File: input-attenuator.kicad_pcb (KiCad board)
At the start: 2 copper layers, 90.2 x 55.8 mm, 100 parts, among them J1 DC_INTF, J2 DC_INTF, J3 RX, J4 ANT, J5 TX, K1 EE2-5TNU-L, K2 EE2-5TNU-L, K3 EE2-5TNU-L, K4 EE2-5TNU-L, Q1 BC858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

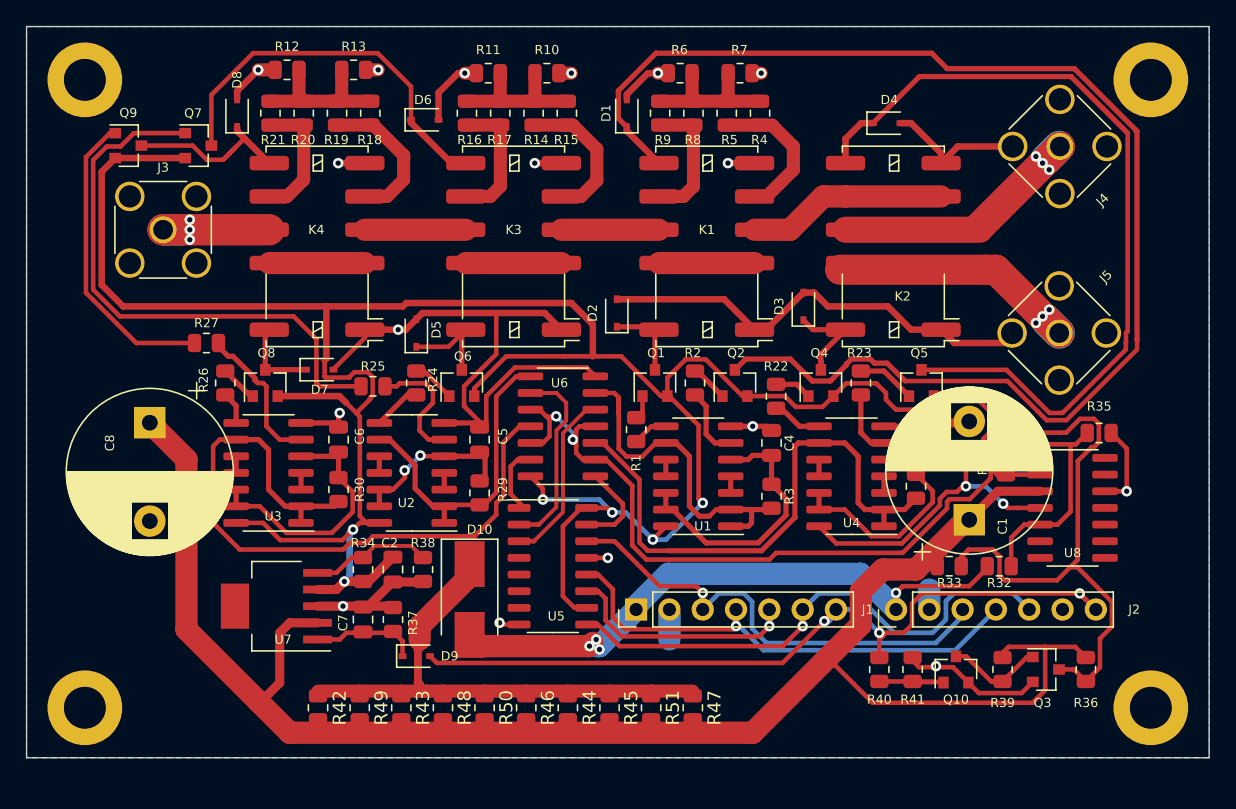
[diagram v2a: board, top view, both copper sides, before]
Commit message: Added regulator heat sink tab and module description on FCu
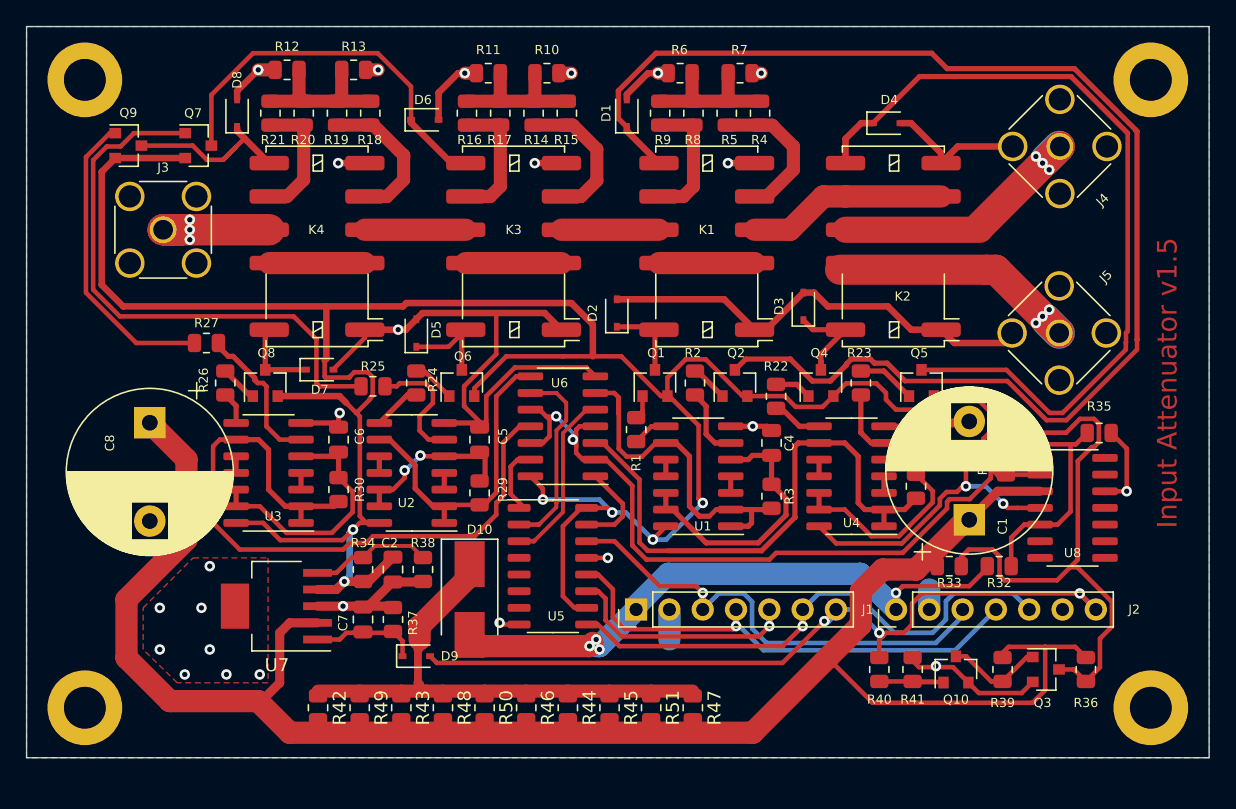
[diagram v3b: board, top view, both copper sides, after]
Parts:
- U7: footprint Package_TO_SOT_SMD:SOT-223-6 -> Package_TO_SOT_SMD:SOT-223-6_TabPin3
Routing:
- net /Vin2: track 135.0 -> 140.4 mm
- net GND: vias 17 -> 25
- added copper zone on F.Cu, net GND
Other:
- board text added: "Input Attenuator v1.5"
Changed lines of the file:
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@@
     )
   )
-  (footprint "Package_TO_SOT_SMD:SOT-223-6" (layer "F.Cu")
+  (footprint "Package_TO_SOT_SMD:SOT-223-6_TabPin3" (layer "F.Cu")
     (at 82.55 69.088 180)
     (descr "module CMS SOT223 6 pins, http://www.ti.com/lit/ds/symlink/tps737.pdf")
@@
     (property "Sheetname" "")
     (attr smd)
-    (fp_text reference "U7" (at -0.508 -2.54) (layer "F.SilkS")
-      (effects (font (size 0.7 0.7) (thickness 0.12)))
+    (fp_text reference "U7" (at -0.0375 -4.5 180) (layer "F.SilkS")
+      (effects (font (size 1 1) (thickness 0.15)))
     )
-    (fp_text value "TPS7A4501DCQT" (at -0.0375 4.5) (layer "F.Fab")
+    (fp_text value "TPS7A4501DCQT" (at -0.0375 4.5 180) (layer "F.Fab")
       (effects (font (size 1 1) (thickness 0.15)))
     )
-    (fp_text user "${REFERENCE}" (at 0 0 90) (layer "F.Fab")
-      (effects (font (size 0.7 0.7) (thickness 0.12)))
+    (fp_text user "${REFERENCE}" (at 0 0 270) (layer "F.Fab")
+      (effects (font (size 0.8 0.8) (thickness 0.12)))
     )
-    (fp_line (start -4.1375 -3.41) (end 1.8725 -3.41) (layer "F.SilkS") (width 0.12))
-    (fp_line (start 1.8725 3.41) (end 1.8725 2.15) (layer "F.SilkS") (width 0.12))
     (fp_line (start 1.8725 -3.41) (end 1.8725 -2.15) (layer "F.SilkS") (width 0.12))
+    (fp_line (start -4.1375 -3.41) (end 1.8725 -3.41) (layer "F.SilkS") (width 0.12))
     (fp_line (start -1.8875 3.41) (end 1.8725 3.41) (layer "F.SilkS") (width 0.12))
-    (fp_line (start 4.49 3.6) (end 4.49 -3.6) (layer "F.CrtYd") (width 0.05))
+    (fp_line (start 1.8725 3.41) (end 1.8725 2.15) (layer "F.SilkS") (width 0.12))
     (fp_line (start -4.49 -3.6) (end -4.49 3.6) (layer "F.CrtYd") (width 0.05))
-    (fp_line (start 4.49 3.6) (end -4.49 3.6) (layer "F.CrtYd") (width 0.05))
     (fp_line (start -4.49 -3.6) (end 4.49 -3.6) (layer "F.CrtYd") (width 0.05))
+    (fp_line (start 4.49 3.6) (end 4.49 -3.6) (layer "F.CrtYd") (width 0.05))
+    (fp_line (start 4.49 3.6) (end -4.49 3.6) (layer "F.CrtYd") (width 0.05))
+    (fp_line (start -0.8375 -3.35) (end 1.8125 -3.35) (layer "F.Fab") (width 0.1))
     (fp_line (start -1.8875 -2.3) (end -1.8875 3.35) (layer "F.Fab") (width 0.1))
     (fp_line (start 1.8125 -3.35) (end 1.8125 3.35) (layer "F.Fab") (width 0.1))
-    (fp_line (start -0.8375 -3.35) (end 1.8125 -3.35) (layer "F.Fab") (width 0.1))
     (fp_line (start -1.8875 3.35) (end 1.8125 3.35) (layer "F.Fab") (width 0.1))
     (fp_line (start -1.8875 -2.3) (end -0.8375 -3.35) (layer "F.Fab") (width 0.1))
@@
     (pad "3" smd rect (at -3.1375 0 180) (locked) (size 2.2 0.6) (layers "F.Cu" "F.Paste" "F.Mask")
       (net 11 "GND") (pinfunction "GND") (pintype "power_in"))
+    (pad "3" smd rect (at 3.1625 0 180) (locked) (size 2.15 3.45) (layers "F.Cu" "F.Paste" "F.Mask")
+      (net 11 "GND") (pinfunction "GND") (pintype "power_in"))
     (pad "4" smd rect (at -3.1375 1.27 180) (locked) (size 2.2 0.6) (layers "F.Cu" "F.Paste" "F.Mask")
       (net 1 "+5V") (pinfunction "OUT") (pintype "power_out"))
     (pad "5" smd rect (at -3.1375 2.54 180) (locked) (size 2.2 0.6) (layers "F.Cu" "F.Paste" "F.Mask")
       (net 81 "Net-(R34-Pad1)") (pinfunction "ADJ") (pintype "bidirectional"))
-    (pad "6" smd rect (at 3.1625 0 180) (locked) (size 2.15 3.45) (layers "F.Cu" "F.Paste" "F.Mask"))
-    (model "${KISYS3DMOD}/Package_TO_SOT_SMD.3dshapes/SOT-223-6.wrl"
+    (model "${KICAD6_3DMODEL_DIR}/Package_TO_SOT_SMD.3dshapes/SOT-223-6.wrl"
       (offset (xyz 0 0 0))
       (scale (xyz 1 1 1))
@@
     (fp_circle (center 0 0) (end 3.1 0) (layer "F.CrtYd") (width 0.05) (fill none))
     (pad "1" thru_hole circle (at 0 0) (locked) (size 5.7 5.7) (drill 3.2) (layers *.Cu *.Mask)
-      (net 11 "GND") (pinfunction "1"))
+      (net 11 "GND") (pinfunction "1") (pintype "input"))
   )
   (footprint "Diode_SMD:D_SOD-323" (layer "F.Cu")
@@
   )
   (gr_rect (start 63.5 24.892) (end 153.67 80.645) (layer "Edge.Cuts") (width 0.05) (fill none))
+  (gr_text "Input Attenuator v1.5" (at 150.495 52.07 90) (layer "F.Cu")
+    (effects (font (size 1.5 1.5) (thickness 0.3)))
+  )
   (segment (start 90.4 62.738) (end 89.425 62.738) (width 0.35) (layer "F.Cu") (net 1))
   (segment (start 106.207 61.595) (end 105.791 61.595) (width 0.35) (layer "F.Cu") (net 1))
@@
   (segment (start 141.171011 72.188989) (end 138.377011 72.188989) (width 0.35) (layer "F.Cu") (net 4))
   (segment (start 127.117011 70.494989) (end 124.587 73.025) (width 1.7) (layer "F.Cu") (net 4))
-  (segment (start 72.898 55.100041) (end 75.692 57.894041) (width 1.7) (layer "F.Cu") (net 4))
+  (segment (start 71.12 73.025) (end 74.422 76.327) (width 1.7) (layer "F.Cu") (net 4))
   (segment (start 138.377011 72.188989) (end 137.922 72.644) (width 0.35) (layer "F.Cu") (net 4))
+  (segment (start 72.898 55.100041) (end 75.692 57.894041) (width 1.7) (layer "F.Cu") (net 4))
   (segment (start 128.016 76.454) (end 124.587 73.025) (width 0.35) (layer "F.Cu") (net 4))
   (segment (start 83.566 70.358) (end 82.804 71.12) (width 0.7) (layer "F.Cu") (net 4))
   (segment (start 141.171011 72.188989) (end 141.171011 75.490989) (width 0.35) (layer "F.Cu") (net 4))
-  (segment (start 75.692 70.866) (end 75.692 64.008) (width 1.7) (layer "F.Cu") (net 4))
   (segment (start 143.459489 72.188989) (end 141.171011 72.188989) (width 0.35) (layer "F.Cu") (net 4))
+  (segment (start 75.692 57.894041) (end 75.692 64.008) (width 1.7) (layer "F.Cu") (net 4))
   (segment (start 144.272 73.0015) (end 143.459489 72.188989) (width 0.35) (layer "F.Cu") (net 4))
   (segment (start 128.778 66.294) (end 127.117011 67.954989) (width 1.7) (layer "F.Cu") (net 4))
@@
   (segment (start 118.872 78.74) (end 83.566 78.74) (width 1.7) (layer "F.Cu") (net 4))
   (segment (start 131.318 66.294) (end 128.778 66.294) (width 1.7) (layer "F.Cu") (net 4))
+  (segment (start 74.422 76.327) (end 81.153 76.327) (width 1.7) (layer "F.Cu") (net 4))
   (segment (start 140.208 76.454) (end 128.016 76.454) (width 0.35) (layer "F.Cu") (net 4))
-  (segment (start 75.692 66.294) (end 75.692 64.008) (width 0.7) (layer "F.Cu") (net 4))
+  (segment (start 71.12 68.58) (end 71.12 73.025) (width 1.7) (layer "F.Cu") (net 4))
   (segment (start 85.6875 70.358) (end 83.566 70.358) (width 0.7) (layer "F.Cu") (net 4))
   (segment (start 81.407 76.327) (end 81.153 76.327) (width 0.25) (layer "F.Cu") (net 4))
@@
   (segment (start 83.566 78.74) (end 81.153 76.327) (width 1.7) (layer "F.Cu") (net 4))
   (segment (start 127.117011 67.954989) (end 127.117011 70.494989) (width 1.7) (layer "F.Cu") (net 4))
+  (segment (start 75.692 64.008) (end 71.12 68.58) (width 1.7) (layer "F.Cu") (net 4))
   (segment (start 135.382 62.501959) (end 137.558959 60.325) (width 0.7) (layer "F.Cu") (net 4))
-  (segment (start 75.692 57.894041) (end 75.692 64.008) (width 1.7) (layer "F.Cu") (net 4))
-  (segment (start 81.153 76.327) (end 75.692 70.866) (width 1.7) (layer "F.Cu") (net 4))
   (segment (start 137.922 72.644) (end 137.922 73.0015) (width 0.35) (layer "F.Cu") (net 4))
   (segment (start 137.558959 60.325) (end 140.781 60.325) (width 0.7) (layer "F.Cu") (net 4))
@@
   (via (at 87.262 35.306) (size 0.8) (drill 0.4) (layers "F.Cu" "B.Cu") (net 11))
   (via (at 119.52 28.448) (size 0.8) (drill 0.4) (layers "F.Cu" "B.Cu") (net 11))
+  (via (at 75.565 74.295) (size 0.8) (drill 0.4) (layers "F.Cu" "B.Cu") (free) (net 11))
   (via (at 99.568 70.358) (size 0.8) (drill 0.4) (layers "F.Cu" "B.Cu") (net 11))
+  (via (at 73.66 72.39) (size 0.8) (drill 0.4) (layers "F.Cu" "B.Cu") (free) (net 11))
+  (via (at 73.66 69.215) (size 0.8) (drill 0.4) (layers "F.Cu" "B.Cu") (free) (net 11))
   (via (at 105.042 28.448) (size 0.8) (drill 0.4) (layers "F.Cu" "B.Cu") (net 11))
+  (via (at 77.47 66.04) (size 0.8) (drill 0.4) (layers "F.Cu" "B.Cu") (free) (net 11))
   (via (at 87.376 54.356) (size 0.8) (drill 0.4) (layers "F.Cu" "B.Cu") (net 11))
   (via (at 147.385 60.325) (size 0.8) (drill 0.4) (layers "F.Cu" "B.Cu") (net 11))
+  (via (at 81.28 74.295) (size 0.8) (drill 0.4) (layers "F.Cu" "B.Cu") (free) (net 11))
   (via (at 96.914 28.448) (size 0.8) (drill 0.4) (layers "F.Cu" "B.Cu") (net 11))
+  (via (at 76.835 69.215) (size 0.8) (drill 0.4) (layers "F.Cu" "B.Cu") (free) (net 11))
   (via (at 102.248 35.306) (size 0.8) (drill 0.4) (layers "F.Cu" "B.Cu") (net 11))
   (via (at 90.31 28.194) (size 0.8) (drill 0.4) (layers "F.Cu" "B.Cu") (net 11))
   (via (at 81.166 28.194) (size 0.8) (drill 0.4) (layers "F.Cu" "B.Cu") (net 11))
   (via (at 87.63 69.088) (size 0.8) (drill 0.4) (layers "F.Cu" "B.Cu") (net 11))
+  (via (at 77.47 72.39) (size 0.8) (drill 0.4) (layers "F.Cu" "B.Cu") (free) (net 11))
+  (via (at 78.74 74.295) (size 0.8) (drill 0.4) (layers "F.Cu" "B.Cu") (free) (net 11))
   (via (at 118.872 55.372) (size 0.8) (drill 0.4) (layers "F.Cu" "B.Cu") (net 11))
   (via (at 91.834 48.006) (size 0.8) (drill 0.4) (layers "F.Cu" "B.Cu") (net 11))
@@
   (segment (start 92.075 75.565) (end 93.98 75.565) (width 1) (layer "F.Cu") (net 83))
   (segment (start 97.282 66.896) (end 97.188 66.896) (width 1.7) (layer "F.Cu") (net 83))
+  (zone (net 11) (net_name "GND") (layer "F.Cu") (hatch edge 0.508)
+    (connect_pads (clearance 0.508))
+    (min_thickness 0.254) (filled_areas_thickness no)
+    (fill yes (thermal_gap 0.508) (thermal_bridge_width 0.508))
+    (polygon
+      (pts
+        (xy 81.915 74.93)
+        (xy 74.990118 74.93)
+        (xy 72.39 72.39)
+        (xy 72.39 69.215)
+        (xy 76.2 65.405)
+        (xy 81.915 65.405)
+      )
+    )
+  )
   (zone (net 11) (net_name "GND") (layer "B.Cu") (hatch edge 0.508)
     (connect_pads (clearance 0.508))

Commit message: Layout: added version and date
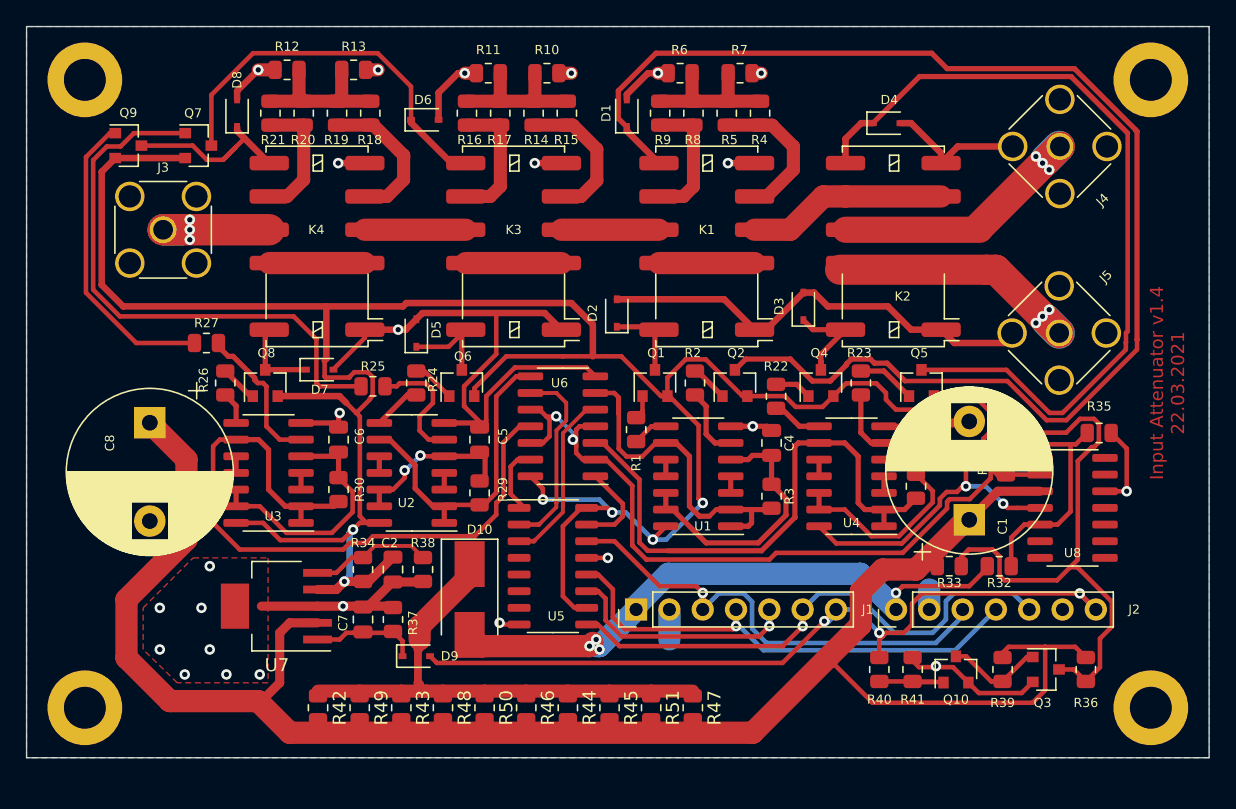
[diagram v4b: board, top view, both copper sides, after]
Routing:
- net GND: track 162.7 -> 167.2 mm
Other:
- board text added: "Input Attenuator v1.4 22.03.2021"
- board text removed: "Input Attenuator v1.5"
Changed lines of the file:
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@@
   )
   (gr_rect (start 63.5 24.892) (end 153.67 80.645) (layer "Edge.Cuts") (width 0.05) (fill none))
-  (gr_text "Input Attenuator v1.5" (at 150.495 52.07 90) (layer "F.Cu")
-    (effects (font (size 1.5 1.5) (thickness 0.3)))
+  (gr_text "Input Attenuator v1.4\n22.03.2021" (at 150.495 52.07 90) (layer "F.Cu")
+    (effects (font (size 1 1) (thickness 0.2)))
   )
   (segment (start 90.4 62.738) (end 89.425 62.738) (width 0.35) (layer "F.Cu") (net 1))
@@
   (segment (start 98.552 54.93) (end 98.044 55.438) (width 0.35) (layer "F.Cu") (net 11))
   (segment (start 89.294 48.006) (end 91.834 48.006) (width 0.5) (layer "F.Cu") (net 11))
+  (segment (start 85.6875 69.088) (end 81.407 69.088) (width 0.7) (layer "F.Cu") (net 11))
   (segment (start 119.012 35.306) (end 116.98 35.306) (width 0.5) (layer "F.Cu") (net 11))
   (segment (start 82.4505 28.194) (end 81.166 28.194) (width 1) (layer "F.Cu") (net 11))
@@
   (segment (start 84.428 55.118) (end 86.967 55.118) (width 0.4) (layer "F.Cu") (net 11))
   (segment (start 112.4225 28.448) (end 111.646 28.448) (width 1) (layer "F.Cu") (net 11))
+  (segment (start 81.407 69.088) (end 81.28 69.215) (width 0.25) (layer "F.Cu") (net 11))
   (segment (start 89.294 35.306) (end 87.262 35.306) (width 0.5) (layer "F.Cu") (net 11))
   (segment (start 104.28 48.006) (end 103.01 46.736) (width 0.5) (layer "F.Cu") (net 11))
